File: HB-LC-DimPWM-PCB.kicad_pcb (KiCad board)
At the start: 2 copper layers, 73 parts, among them J1 SWD, J3 Conn_01x04_Male, Q1 S9013, Q10 BSS84, Q11 2N7002, Q12 BSS84, Q13 2N7002, Q14 VS5810AS, Q15 VS5810AS, Q16 VS5810AS, Q2 BSS84, Q3 2N7002, Q4 VS5810AS, Q5 S9013, Q6 S9013, Q7 S9013, Q8 BSS84, Q9 2N7002, U1 STM32F103C8Tx, U2 AMS1117-3.3, Y1 8MHz

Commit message: Add alternate gate driver setup
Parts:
- added C25: 1uF, Capacitor_SMD:C_0402_1005Metric, F.Cu at (114.9, 101.0)
- added C26: 1uF, Capacitor_SMD:C_0402_1005Metric, F.Cu at (114.9, 106.4)
- added C27: 1uF, Capacitor_SMD:C_0402_1005Metric, F.Cu at (114.9, 111.8)
- added C28: 1uF, Capacitor_SMD:C_0402_1005Metric, F.Cu at (114.9, 117.2)
- added C29: 100n, Capacitor_SMD:C_0603_1608Metric, F.Cu at (117.4, 101.0)
- added C30: 100n, Capacitor_SMD:C_0603_1608Metric, F.Cu at (117.4, 106.4)
- added C31: 100n, Capacitor_SMD:C_0603_1608Metric, F.Cu at (117.4, 111.8)
- added C32: 100n, Capacitor_SMD:C_0603_1608Metric, F.Cu at (117.4, 117.2)
- added C33: 100p, Capacitor_SMD:C_0402_1005Metric, F.Cu at (286.6, 134.2)
- added C34: 100p, Capacitor_SMD:C_0402_1005Metric, F.Cu at (271.7, 149.4)
- added C35: 100p, Capacitor_SMD:C_0402_1005Metric, F.Cu at (264.9, 155.8)
- added C36: 100p, Capacitor_SMD:C_0402_1005Metric, F.Cu at (282.8, 137.8)
- added C37: 1uF, Capacitor_SMD:C_0603_1608Metric, F.Cu at (222.8, 161.5)
- added C38: 1uF, Capacitor_SMD:C_0603_1608Metric, F.Cu at (229.4, 161.5)
- added C39: 1uF, Capacitor_SMD:C_0603_1608Metric, F.Cu at (151.6, 111.0)
- added C40: 1uF, Capacitor_SMD:C_0603_1608Metric, F.Cu at (256.6, 160.5)
- added C41: 1uF, Capacitor_SMD:C_0402_1005Metric, F.Cu at (299.3, 121.1)
- added C42: 1uF, Capacitor_SMD:C_0402_1005Metric, F.Cu at (278.4, 141.9)
- added C43: 1uF, Capacitor_SMD:C_0402_1005Metric, F.Cu at (295.0, 125.7)
- added C44: 1uF, Capacitor_SMD:C_0402_1005Metric, F.Cu at (298.5, 123.1)
- added C45: 1uF, Capacitor_SMD:C_0402_1005Metric, F.Cu at (271.7, 147.4)
- added C46: 1uF, Capacitor_SMD:C_0402_1005Metric, F.Cu at (267.8, 153.3)
- added C47: 1uF, Capacitor_SMD:C_0402_1005Metric, F.Cu at (277.3, 144.4)
- added C48: 1uF, Capacitor_SMD:C_0402_1005Metric, F.Cu at (274.6, 146.4)
- added C49: 100n, Capacitor_SMD:C_0603_1608Metric, F.Cu at (274.9, 142.2)
- added C50: 100n, Capacitor_SMD:C_0603_1608Metric, F.Cu at (261.4, 156.6)
- added C51: 100n, Capacitor_SMD:C_0603_1608Metric, F.Cu at (291.5, 126.0)
- added C52: 100n, Capacitor_SMD:C_0603_1608Metric, F.Cu at (268.2, 149.1)
- added C53: 100n, Capacitor_SMD:C_0603_1608Metric, F.Cu at (198.7, 161.5)
- added C54: 100n, Capacitor_SMD:C_0603_1608Metric, F.Cu at (233.4, 161.5)
- added C55: 100n, Capacitor_SMD:C_0603_1608Metric, F.Cu at (283.1, 133.6)
- added C56: 100n, Capacitor_SMD:C_0603_1608Metric, F.Cu at (279.3, 137.5)
- added C57: 100p, Capacitor_SMD:C_0402_1005Metric, F.Cu at (282.8, 135.8)
- added C58: 100p, Capacitor_SMD:C_0402_1005Metric, F.Cu at (267.7, 151.3)
- added C59: 100p, Capacitor_SMD:C_0402_1005Metric, F.Cu at (286.6, 132.2)
- added C60: 100p, Capacitor_SMD:C_0402_1005Metric, F.Cu at (296.4, 121.1)
- added C61: 100p, Capacitor_SMD:C_0402_1005Metric, F.Cu at (286.6, 130.2)
- added C62: 100p, Capacitor_SMD:C_0402_1005Metric, F.Cu at (278.8, 139.8)
- added C63: 100p, Capacitor_SMD:C_0402_1005Metric, F.Cu at (264.9, 153.8)
- added C64: 100p, Capacitor_SMD:C_0402_1005Metric, F.Cu at (274.4, 144.4)
- added C65: 1uF, Capacitor_SMD:C_0603_1608Metric, F.Cu at (270.9, 145.1)
- added C66: 1uF, Capacitor_SMD:C_0603_1608Metric, F.Cu at (202.7, 161.5)
- added C67: 1uF, Capacitor_SMD:C_0603_1608Metric, F.Cu at (264.2, 151.6)
- added C68: 1uF, Capacitor_SMD:C_0603_1608Metric, F.Cu at (283.1, 131.1)
- added C69: 1uF, Capacitor_SMD:C_0603_1608Metric, F.Cu at (297.0, 118.8)
- added C70: 1uF, Capacitor_SMD:C_0603_1608Metric, F.Cu at (270.9, 142.6)
- added C71: 1uF, Capacitor_SMD:C_0603_1608Metric, F.Cu at (292.1, 123.5)
- added C72: 1uF, Capacitor_SMD:C_0603_1608Metric, F.Cu at (264.2, 149.1)
- added F10: 15V 5A, Fuse:Fuse_2920_7451Metric, F.Cu at (276.5, 115.2)
- added F11: 15V 5A, Fuse:Fuse_2920_7451Metric, F.Cu at (243.8, 151.6)
- added F12: 15V 5A, Fuse:Fuse_2920_7451Metric, F.Cu at (254.1, 144.6)
- added F13: 15V 5A, Fuse:Fuse_2920_7451Metric, F.Cu at (201.8, 156.8)
- added F14: 15V 5A, Fuse:Fuse_2920_7451Metric, F.Cu at (212.1, 156.8)
- added F15: 15V 5A, Fuse:Fuse_2920_7451Metric, F.Cu at (222.3, 156.8)
- added F16: 15V 5A, Fuse:Fuse_2920_7451Metric, F.Cu at (274.8, 108.2)
- added F17: 15V 5A, Fuse:Fuse_2920_7451Metric, F.Cu at (266.3, 120.3)
- added F6: 15V 5A, Fuse:Fuse_2920_7451Metric, F.Cu at (157.8, 120.0)
- added F7: 15V 5A, Fuse:Fuse_2920_7451Metric, F.Cu at (157.8, 114.0)
- added F8: 15V 5A, Fuse:Fuse_2920_7451Metric, F.Cu at (157.8, 108.0)
- added F9: 15V 5A, Fuse:Fuse_2920_7451Metric, F.Cu at (157.8, 102.0)
- added J4: Conn_01x04_Male, Connector_Phoenix_MC_HighVoltage:PhoenixContact_MC_1,5_4-G-5.08_1x04_P5.08mm_Horizontal, F.Cu at (165.1, 118.5)
- added J5: Conn_01x04_Male, Connector_Phoenix_MC_HighVoltage:PhoenixContact_MC_1,5_4-G-5.08_1x04_P5.08mm_Horizontal, F.Cu at (200.4, 120.0)
- added J6: Conn_01x04_Male, Connector_Phoenix_MC_HighVoltage:PhoenixContact_MC_1,5_4-G-5.08_1x04_P5.08mm_Horizontal, F.Cu at (222.8, 107.8)
- added L10: 3.3uH, Inductor_Sunlord:SMD-PIND-10.5x11.5x4_2.5x3.0, F.Cu at (217.7, 147.2)
- added L11: 3.3uH, Inductor_Sunlord:SMD-PIND-10.5x11.5x4_2.5x3.0, F.Cu at (203.7, 135.1)
- added L12: 3.3uH, Inductor_Sunlord:SMD-PIND-10.5x11.5x4_2.5x3.0, F.Cu at (231.7, 135.0)
- added L13: 3.3uH, Inductor_Sunlord:SMD-PIND-10.5x11.5x4_2.5x3.0, F.Cu at (262.6, 110.7)
- added L14: 3.3uH, Inductor_Sunlord:SMD-PIND-10.5x11.5x4_2.5x3.0, F.Cu at (231.7, 147.2)
- added L15: 3.3uH, Inductor_Sunlord:SMD-PIND-10.5x11.5x4_2.5x3.0, F.Cu at (254.2, 122.9)
- added L16: 3.3uH, Inductor_Sunlord:SMD-PIND-10.5x11.5x4_2.5x3.0, F.Cu at (245.7, 135.0)
- added L5: 3.3uH, Inductor_Sunlord:SMD-PIND-10.5x11.5x4_2.5x3.0, F.Cu at (146.5, 117.3)
- added L6: 3.3uH, Inductor_Sunlord:SMD-PIND-10.5x11.5x4_2.5x3.0, F.Cu at (133.0, 117.3)
- added L7: 3.3uH, Inductor_Sunlord:SMD-PIND-10.5x11.5x4_2.5x3.0, F.Cu at (132.9, 104.8)
- added L8: 3.3uH, Inductor_Sunlord:SMD-PIND-10.5x11.5x4_2.5x3.0, F.Cu at (146.5, 104.8)
- added L9: 3.3uH, Inductor_Sunlord:SMD-PIND-10.5x11.5x4_2.5x3.0, F.Cu at (240.2, 122.9)
- added Q17: VS5810AS, Package_SO:SOIC-8_3.9x4.9mm_P1.27mm, F.Cu at (122.6, 119.1)
- added Q18: VS5810AS, Package_SO:SOIC-8_3.9x4.9mm_P1.27mm, F.Cu at (122.6, 113.7)
- added Q19: VS5810AS, Package_SO:SOIC-8_3.9x4.9mm_P1.27mm, F.Cu at (122.6, 108.3)
- added Q20: VS5810AS, Package_SO:SOIC-8_3.9x4.9mm_P1.27mm, F.Cu at (122.6, 102.9)
- added Q21: VS5810AS, Package_SO:SOIC-8_3.9x4.9mm_P1.27mm, F.Cu at (275.6, 128.4)
- added Q22: VS5810AS, Package_SO:SOIC-8_3.9x4.9mm_P1.27mm, F.Cu at (285.9, 121.4)
- added Q23: VS5810AS, Package_SO:SOIC-8_3.9x4.9mm_P1.27mm, F.Cu at (294.4, 114.3)
- added Q24: VS5810AS, Package_SO:SOIC-8_3.9x4.9mm_P1.27mm, F.Cu at (267.2, 127.0)
- added Q25: VS5810AS, Package_SO:SOIC-8_3.9x4.9mm_P1.27mm, F.Cu at (263.4, 139.9)
- added Q26: VS5810AS, Package_SO:SOIC-8_3.9x4.9mm_P1.27mm, F.Cu at (267.2, 133.5)
- added Q27: VS5810AS, Package_SO:SOIC-8_3.9x4.9mm_P1.27mm, F.Cu at (275.6, 121.9)
- added Q28: VS5810AS, Package_SO:SOIC-8_3.9x4.9mm_P1.27mm, F.Cu at (294.4, 107.9)
- added R20: 10k, Resistor_SMD:R_0402_1005Metric, F.Cu at (114.7, 119.3)
- added R21: 10k, Resistor_SMD:R_0402_1005Metric, F.Cu at (114.7, 113.9)
- added R22: 10k, Resistor_SMD:R_0402_1005Metric, F.Cu at (114.7, 108.5)
- added R23: 10k, Resistor_SMD:R_0402_1005Metric, F.Cu at (114.7, 103.1)
- added R24: 10k, Resistor_SMD:R_0402_1005Metric, F.Cu at (242.7, 162.6)
- added R25: 10k, Resistor_SMD:R_0402_1005Metric, F.Cu at (245.6, 162.6)
- added R26: 10k, Resistor_SMD:R_0402_1005Metric, F.Cu at (248.6, 162.6)
- added R27: 10k, Resistor_SMD:R_0402_1005Metric, F.Cu at (236.9, 162.6)
- added R28: 10k, Resistor_SMD:R_0402_1005Metric, F.Cu at (289.5, 130.2)
- added R29: 10k, Resistor_SMD:R_0402_1005Metric, F.Cu at (260.9, 158.8)
- added R30: 10k, Resistor_SMD:R_0402_1005Metric, F.Cu at (295.6, 123.2)
- added R31: 10k, Resistor_SMD:R_0402_1005Metric, F.Cu at (291.0, 128.2)
- added U10: MCP1416, Package_TO_SOT_SMD:SOT-23-5, F.Cu at (270.1, 139.0)
- added U11: MCP1416, Package_TO_SOT_SMD:SOT-23-5, F.Cu at (255.1, 138.2)
- added U12: MCP1416, Package_TO_SOT_SMD:SOT-23-5, F.Cu at (259.8, 150.4)
- added U13: MCP1416, Package_TO_SOT_SMD:SOT-23-5, F.Cu at (273.8, 133.9)
- added U14: MCP1416, Package_TO_SOT_SMD:SOT-23-5, F.Cu at (261.6, 145.5)
- added U3: MCP1416, Package_TO_SOT_SMD:SOT-23-5, F.Cu at (117.1, 119.9)
- added U4: MCP1416, Package_TO_SOT_SMD:SOT-23-5, F.Cu at (117.1, 114.5)
- added U5: MCP1416, Package_TO_SOT_SMD:SOT-23-5, F.Cu at (117.1, 109.1)
- added U6: MCP1416, Package_TO_SOT_SMD:SOT-23-5, F.Cu at (117.1, 103.7)
- added U7: MCP1416, Package_TO_SOT_SMD:SOT-23-5, F.Cu at (278.7, 133.9)
- added U8: MCP1416, Package_TO_SOT_SMD:SOT-23-5, F.Cu at (292.5, 119.9)
- added U9: MCP1416, Package_TO_SOT_SMD:SOT-23-5, F.Cu at (282.3, 127.5)
- R14, R15, R16, R17, R18, R19, R6, R7: footprint Resistor_SMD:R_0805_2012Metric -> Resistor_SMD:R_0603_1608Metric
- moved F5 99.0 mm to (157.5, 71.0), turned to 180 degrees
- moved J3 96.5 mm to (165.2, 87.8), turned to 90 degrees
- moved F4 87.1 mm to (157.5, 77.1), turned to 180 degrees
- moved C21 82.3 mm to (155.3, 60.8)
- moved L4 81.3 mm to (145.8, 73.8)
- moved R19 71.0 mm to (115.9, 71.1), turned to 180 degrees
- moved R18 66.9 mm to (115.9, 72.6)
- moved F2 63.7 mm to (157.5, 89.3), turned to 180 degrees
- moved F3 63.3 mm to (157.5, 83.2), turned to 180 degrees
- moved R17 60.0 mm to (115.8, 77.9), turned to 180 degrees
- moved Q16 57.0 mm to (121.4, 72.0)
- moved Q4 56.1 mm to (121.4, 88.5)
- moved R16 55.9 mm to (115.8, 79.5)
- moved C24 55.3 mm to (148.0, 66.8), turned to 180 degrees
- moved R9 55.1 mm to (110.0, 75.1), turned to 270 degrees
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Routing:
- net Net-(C23-Pad1): track 0.00 -> 23.6 mm
- net Net-(C22-Pad1): track 0.00 -> 22.5 mm
- net Net-(C17-Pad1): track 0.00 -> 19.5 mm
- net Net-(C20-Pad1): track 0.00 -> 19.4 mm
- net Net-(C19-Pad1): track 0.00 -> 6.68 mm
- net Net-(Q12-Pad1): track 0.00 -> 6.53 mm
- net Net-(C24-Pad1): track 0.00 -> 4.83 mm
- net Net-(C21-Pad1): track 0.00 -> 4.64 mm
- net Net-(Q16-Pad4): track 0.00 -> 4.30 mm
- net Net-(C18-Pad1): track 0.00 -> 4.24 mm
- net Net-(F2-Pad1): track 0.00 -> 4.22 mm
- net Net-(F5-Pad1): track 0.00 -> 4.20 mm
- net Net-(Q11-Pad3): track 0.00 -> 4.03 mm
- net Net-(Q13-Pad3): track 0.00 -> 3.98 mm
- net Net-(F4-Pad1): track 0.00 -> 3.80 mm
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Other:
- net class Default: clearance 0.2 -> 0.127; trace_width 0.25 -> 0.127; via_dia 0.8 -> 0.6; via_drill 0.4 -> 0.43
- rule trace_clearance: 0.2 -> 0.127
- rule trace_min: 0.2 -> 0.127
- rule via_min_size: 0.4 -> 0.6

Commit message: Layout one dimmer channel
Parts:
- removed C25, C26, C27, C28, C41, C42, C43, C44, C45, C46, C47, C48: 1uF, Capacitor_SMD:C_0402_1005Metric
- removed C29, C30, C31, C32, C49, C50, C51, C52, C53, C54, C55, C56: 100n, Capacitor_SMD:C_0603_1608Metric
- removed C33, C34, C35, C36, C57, C58, C59, C60, C61, C62, C63, C64: 100p, Capacitor_SMD:C_0402_1005Metric
- removed C37, C38, C39, C40, C65, C66, C67, C68, C69, C70, C71, C72: 1uF, Capacitor_SMD:C_0603_1608Metric
- removed F10, F11, F12, F13, F14, F15, F16, F17, F6, F7, F8, F9: 15V 5A, Fuse:Fuse_2920_7451Metric
- removed J4, J5, J6: Conn_01x04_Male, Connector_Phoenix_MC_HighVoltage:PhoenixContact_MC_1,5_4-G-5.08_1x04_P5.08mm_Horizontal
- removed L10, L11, L12, L13, L14, L15, L16, L5, L6, L7, L8, L9: 3.3uH, Inductor_Sunlord:SMD-PIND-10.5x11.5x4_2.5x3.0
- removed Q17, Q18, Q19, Q20, Q21, Q22, Q23, Q24, Q25, Q26, Q27, Q28: VS5810AS, Package_SO:SOIC-8_3.9x4.9mm_P1.27mm
- removed R20, R21, R22, R23, R24, R25, R26, R27, R28, R29, R30, R31: 10k, Resistor_SMD:R_0402_1005Metric
- removed U10, U11, U12, U13, U14, U3, U4, U5, U6, U7, U8, U9: MCP1416, Package_TO_SOT_SMD:SOT-23-5
- C17, C18, C19, C20: footprint Capacitor_SMD:C_0402_1005Metric -> Capacitor_SMD:C_0805_2012Metric
- C21, C22, C23, C24: footprint Capacitor_SMD:C_0603_1608Metric -> Capacitor_SMD:C_1206_3216Metric
- moved C18 104.7 mm to (134.7, 80.4)
- moved C17 80.9 mm to (119.9, 92.6), turned to 180 degrees
- moved C20 79.7 mm to (119.9, 67.8), turned to 180 degrees
- moved C19 77.4 mm to (129.3, 80.4)
- moved C21 33.1 mm to (165.2, 92.3)
- moved C24 17.2 mm to (165.2, 68.1), turned to 0 degrees
- moved C22 5.32 mm to (142.3, 80.4)
- moved L1 1.90 mm to (145.8, 88.1)
- moved L2 1.90 mm to (132.1, 88.1)
- moved C23 1.84 mm to (149.4, 80.4)
- moved L3 1.10 mm to (132.2, 72.7)
- moved L4 1.10 mm to (145.9, 72.7)
- moved R14 0.20 mm to (115.9, 86.2)
- moved C13 0.10 mm to (110.0, 90.6)
- moved C14 0.10 mm to (110.0, 83.8)
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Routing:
- net Net-(C22-Pad1): track 22.5 -> 0.00 mm
- net Net-(C23-Pad1): track 23.6 -> 1.12 mm
- net Net-(C17-Pad1): track 19.5 -> 0.00 mm
- net Net-(C20-Pad1): track 19.4 -> 0.00 mm
- net Net-(Q5-Pad3): track 0.00 -> 10.0 mm
- net Net-(Q1-Pad3): track 0.00 -> 10.0 mm
- net Net-(Q10-Pad1): track 0.00 -> 10.0 mm
- net +12V: track 2.49 -> 9.78 mm
- net Net-(C19-Pad1): track 6.68 -> 0.00 mm
- net Net-(C24-Pad1): track 4.83 -> 0.00 mm
- net Net-(C21-Pad1): track 4.64 -> 0.00 mm
- net Net-(Q4-Pad4): track 0.00 -> 4.24 mm
- net Net-(C18-Pad1): track 4.24 -> 0.00 mm
- net Net-(F2-Pad1): track 4.22 -> 0.00 mm
- net Net-(F5-Pad1): track 4.20 -> 0.00 mm
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- added copper zone on F.Cu, net Net-(C17-Pad1)
- added copper zone on F.Cu, net Net-(C18-Pad1)
- added copper zone on F.Cu, net Net-(C19-Pad1)
- added copper zone on F.Cu, net Net-(C20-Pad1)
- added copper zone on F.Cu, net Net-(C21-Pad1)
- added copper zone on F.Cu, net Net-(C22-Pad1)
- added copper zone on F.Cu, net Net-(C23-Pad1)
- added copper zone on F.Cu, net Net-(C24-Pad1)
- added copper zone on F.Cu, net Net-(F2-Pad1)
- added copper zone on F.Cu, net Net-(F3-Pad1)
- added copper zone on F.Cu, net Net-(F4-Pad1)
- added copper zone on F.Cu, net Net-(F5-Pad1)

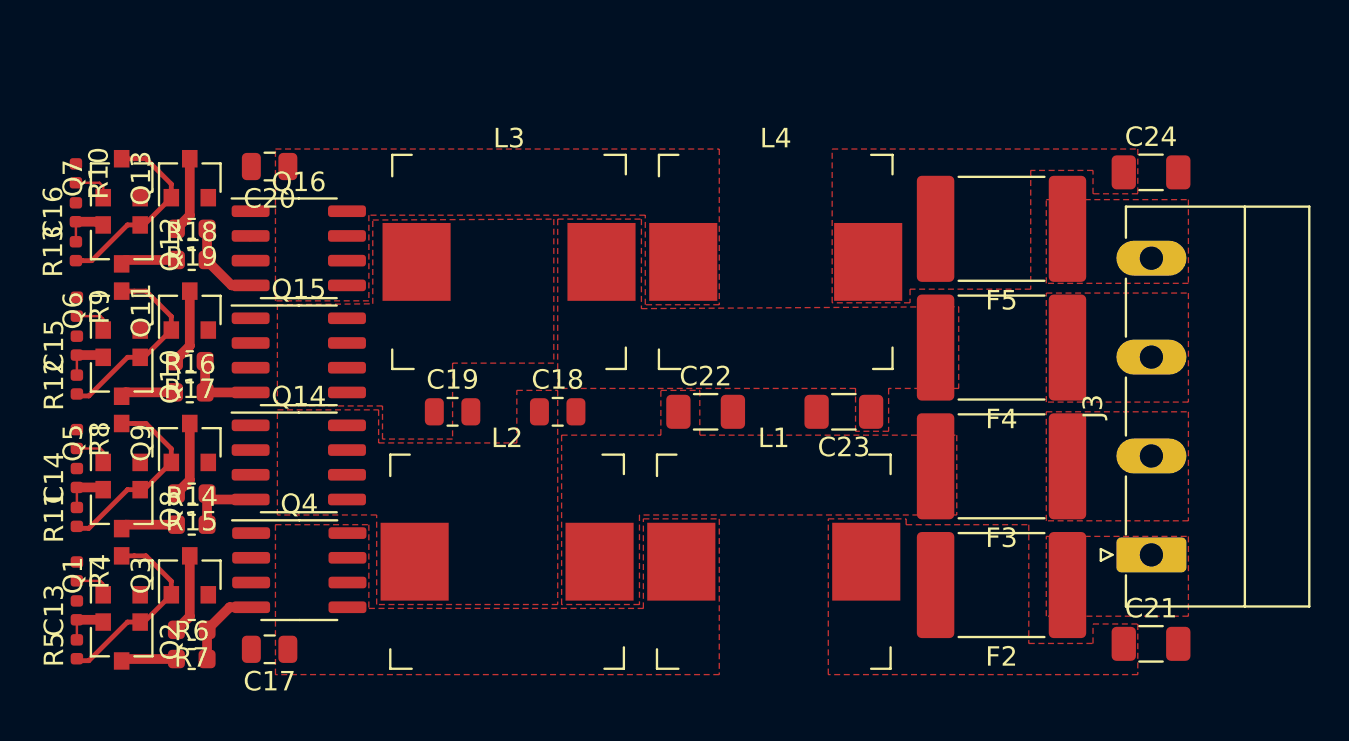
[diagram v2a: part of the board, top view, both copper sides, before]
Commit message: Optimize channel layout
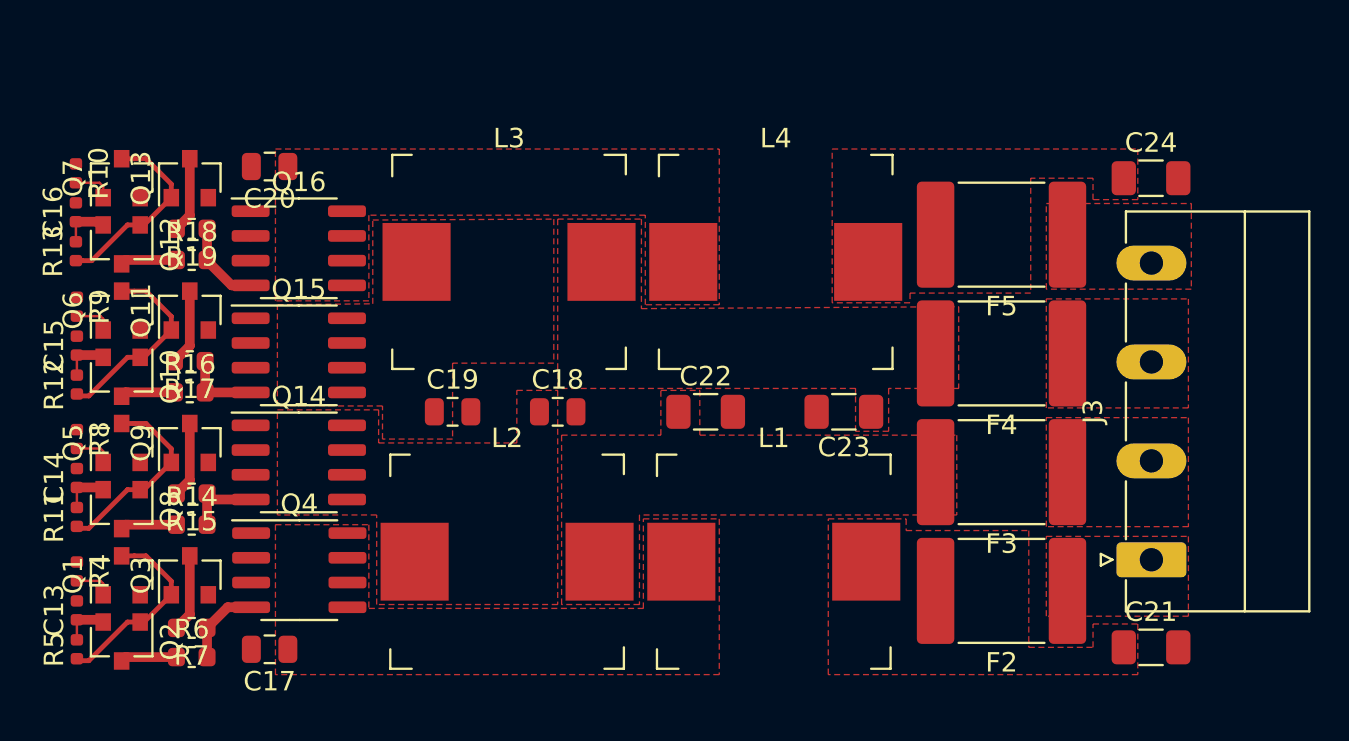
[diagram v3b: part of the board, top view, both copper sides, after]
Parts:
- moved C24 0.30 mm to (165.2, 68.4)
- moved F4 0.30 mm to (157.5, 77.4)
- moved F2 0.30 mm to (157.5, 89.6)
- moved F3 0.30 mm to (157.5, 83.5)
- moved F5 0.30 mm to (157.5, 71.3)
- moved J3 0.25 mm to (165.2, 88.0)
- moved C21 0.18 mm to (165.2, 92.5)
- moved R6 0.10 mm to (115.9, 93.0)
- moved R7 0.10 mm to (115.9, 91.5)
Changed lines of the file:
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@@
   )
   (module Capacitor_SMD:C_1206_3216Metric (layer F.Cu)
-    (at 165.18 68.1)
+    (at 165.18 68.4)
     (descr "Capacitor SMD 1206 (3216 Metric), square (rectangular) end terminal, IPC_7351 nominal, (Body size source: http://www.tortai-tech.com/upload/download/2011102023233369053.pdf), generated with kicad-footprint-generator")
     (tags capacitor)
@@
   )
   (module Capacitor_SMD:C_1206_3216Metric (layer F.Cu)
-    (at 165.18 92.32)
+    (at 165.18 92.5)
     (descr "Capacitor SMD 1206 (3216 Metric), square (rectangular) end terminal, IPC_7351 nominal, (Body size source: http://www.tortai-tech.com/upload/download/2011102023233369053.pdf), generated with kicad-footprint-generator")
     (tags capacitor)
@@
   )
   (module Resistor_SMD:R_0603_1608Metric (layer F.Cu)
-    (at 115.9 93.1)
+    (at 115.9 93)
     (descr "Resistor SMD 0603 (1608 Metric), square (rectangular) end terminal, IPC_7351 nominal, (Body size source: http://www.tortai-tech.com/upload/download/2011102023233369053.pdf), generated with kicad-footprint-generator")
     (tags resistor)
@@
   )
   (module Resistor_SMD:R_0603_1608Metric (layer F.Cu)
-    (at 115.9 91.6 180)
+    (at 115.9 91.5 180)
     (descr "Resistor SMD 0603 (1608 Metric), square (rectangular) end terminal, IPC_7351 nominal, (Body size source: http://www.tortai-tech.com/upload/download/2011102023233369053.pdf), generated with kicad-footprint-generator")
     (tags resistor)
@@
   )
   (module Connector_Phoenix_MC_HighVoltage:PhoenixContact_MC_1,5_4-G-5.08_1x04_P5.08mm_Horizontal (layer F.Cu)
-    (at 165.2 87.75 90)
+    (at 165.2 88 90)
     (descr "Generic Phoenix Contact connector footprint for: MC_1,5/4-G-5.08; number of pins: 04; pin pitch: 5.08mm; Angled || order number: 1836202 8A 320V")
     (tags "phoenix_contact connector MC_01x04_G_5.08mm")
@@
   )
   (module Fuse:Fuse_2920_7451Metric (layer F.Cu)
-    (at 157.5 71 180)
+    (at 157.5 71.3 180)
     (descr "Fuse SMD 2920 (7451 Metric), square (rectangular) end terminal, IPC_7351 nominal, (Body size from: http://www.megastar.com/products/fusetronic/polyswitch/PDF/smd2920.pdf), generated with kicad-footprint-generator")
     (tags resistor)
@@
   )
   (module Fuse:Fuse_2920_7451Metric (layer F.Cu)
-    (at 157.5 77.1 180)
+    (at 157.5 77.4 180)
     (descr "Fuse SMD 2920 (7451 Metric), square (rectangular) end terminal, IPC_7351 nominal, (Body size from: http://www.megastar.com/products/fusetronic/polyswitch/PDF/smd2920.pdf), generated with kicad-footprint-generator")
     (tags resistor)
@@
   )
   (module Fuse:Fuse_2920_7451Metric (layer F.Cu)
-    (at 157.5 83.2 180)
+    (at 157.5 83.5 180)
     (descr "Fuse SMD 2920 (7451 Metric), square (rectangular) end terminal, IPC_7351 nominal, (Body size from: http://www.megastar.com/products/fusetronic/polyswitch/PDF/smd2920.pdf), generated with kicad-footprint-generator")
     (tags resistor)
@@
   )
   (module Fuse:Fuse_2920_7451Metric (layer F.Cu)
-    (at 157.5 89.3 180)
+    (at 157.5 89.6 180)
     (descr "Fuse SMD 2920 (7451 Metric), square (rectangular) end terminal, IPC_7351 nominal, (Body size from: http://www.megastar.com/products/fusetronic/polyswitch/PDF/smd2920.pdf), generated with kicad-footprint-generator")
     (tags resistor)
@@
   (segment (start 111.212 89.085) (end 111.35 89.223) (width 0.127) (layer F.Cu) (net 15))
   (segment (start 110 89.085) (end 111.212 89.085) (width 0.127) (layer F.Cu) (net 15))
-  (segment (start 112.4 93.1) (end 112.3 93.2) (width 0.5) (layer F.Cu) (net 16))
-  (segment (start 115.1125 93.1) (end 112.4 93.1) (width 0.5) (layer F.Cu) (net 16))
-  (segment (start 115.8 90.9125) (end 115.8 87.8) (width 0.5) (layer F.Cu) (net 17))
-  (segment (start 115.1125 91.6) (end 115.8 90.9125) (width 0.5) (layer F.Cu) (net 17))
-  (segment (start 117.8475 90.44) (end 116.6875 91.6) (width 0.5) (layer F.Cu) (net 18))
-  (segment (start 118.95 90.44) (end 117.8475 90.44) (width 0.5) (layer F.Cu) (net 18))
-  (segment (start 116.6875 91.6) (end 116.6875 93.1) (width 0.5) (layer F.Cu) (net 18))
+  (segment (start 112.5 93) (end 112.3 93.2) (width 0.5) (layer F.Cu) (net 16))
+  (segment (start 115.1125 93) (end 112.5 93) (width 0.5) (layer F.Cu) (net 16))
+  (segment (start 115.8 90.8125) (end 115.8 87.8) (width 0.5) (layer F.Cu) (net 17))
+  (segment (start 115.1125 91.5) (end 115.8 90.8125) (width 0.5) (layer F.Cu) (net 17))
+  (segment (start 116.6875 91.5) (end 116.6875 93) (width 0.5) (layer F.Cu) (net 18))
+  (segment (start 117.7475 90.44) (end 116.6875 91.5) (width 0.5) (layer F.Cu) (net 18))
+  (segment (start 118.95 90.44) (end 117.7475 90.44) (width 0.5) (layer F.Cu) (net 18))
   (segment (start 154 78.425) (end 154 77.3) (width 0.75) (layer F.Cu) (net 61))
   (segment (start 112.95 81) (end 112.3 81) (width 0.25) (layer F.Cu) (net 67))
@@
     (polygon
       (pts
-        (xy 167.1 86) (xy 159.8 86) (xy 159.8 80.4) (xy 167.1 80.4)
+        (xy 167.1 86.3) (xy 159.8 86.3) (xy 159.8 80.7) (xy 167.1 80.7)
       )
     )
@@
     (polygon
       (pts
-        (xy 167.1 79.9) (xy 159.8 79.9) (xy 159.8 74.3) (xy 167.1 74.3)
+        (xy 167.1 80.2) (xy 159.8 80.2) (xy 159.8 74.6) (xy 167.1 74.6)
       )
     )
@@
     (polygon
       (pts
-        (xy 167.1 73.8) (xy 159.8 73.8) (xy 159.8 69.5) (xy 167.1 69.5)
+        (xy 167.25 74.1) (xy 159.8 74.1) (xy 159.8 69.7) (xy 167.25 69.7)
       )
     )
@@
     (polygon
       (pts
-        (xy 164.5 69.2) (xy 162.2 69.2) (xy 162.2 68) (xy 159 68) (xy 159 74.1)
-        (xy 152.8 74.1) (xy 152.8 74.8) (xy 148.8 74.8) (xy 148.8 66.9) (xy 164.5 66.9)
+        (xy 164.501736 69.5) (xy 162.198264 69.5) (xy 162.2 68.4) (xy 159 68.4) (xy 159 74.3)
+        (xy 152.8 74.3) (xy 152.8 74.8) (xy 148.8 74.8) (xy 148.8 66.9) (xy 164.5 66.9)
       )
     )
@@
     (polygon
       (pts
-        (xy 152.6 86.2) (xy 158.9 86.2) (xy 158.9 92.3) (xy 162.2 92.3) (xy 162.2 91.3)
+        (xy 152.6 86.5) (xy 158.9 86.5) (xy 158.9 92.5) (xy 162.2 92.5) (xy 162.2 91.3)
         (xy 164.5 91.3) (xy 164.5 93.9) (xy 148.6 93.9) (xy 148.6 85.9) (xy 152.6 85.9)
       )
